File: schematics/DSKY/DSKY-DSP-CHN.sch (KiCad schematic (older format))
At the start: 5 parts, among them U20 74LS273, U21 74LS273, U22 74LS273, U5 74LS04, U7 74LS00

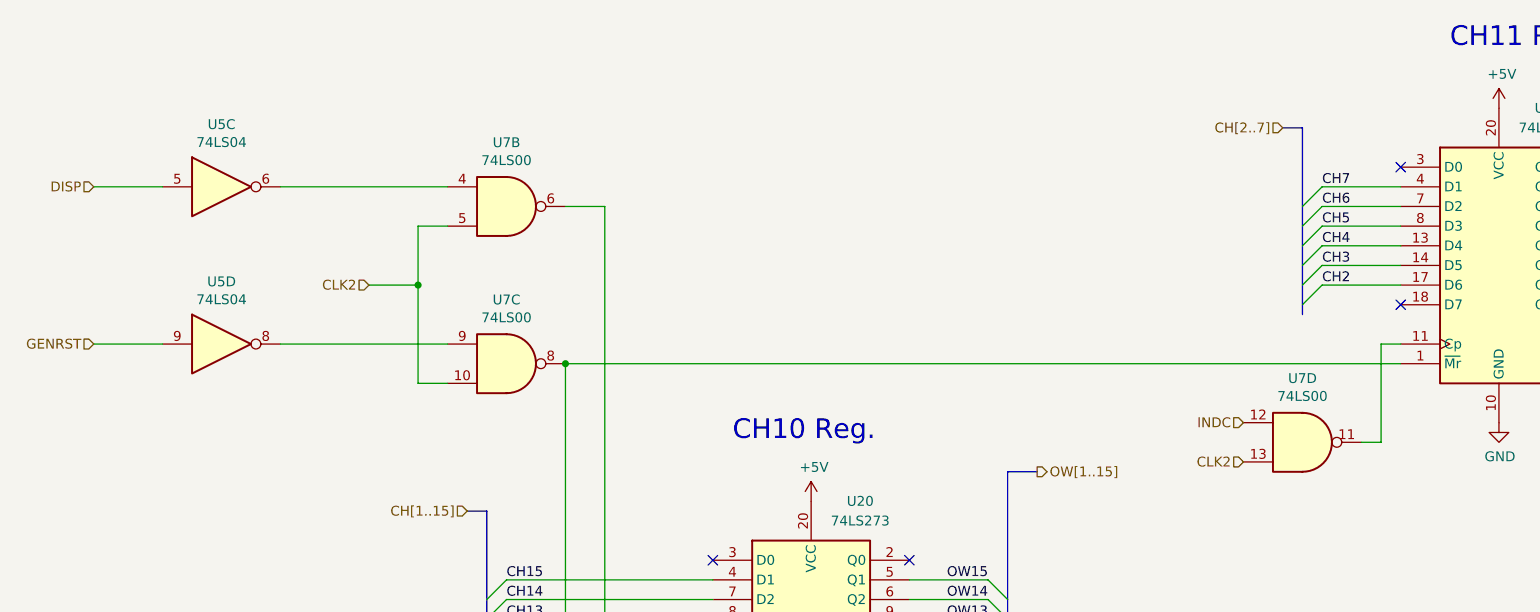
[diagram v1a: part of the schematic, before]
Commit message: Minor tweaks to the display decoding logic.
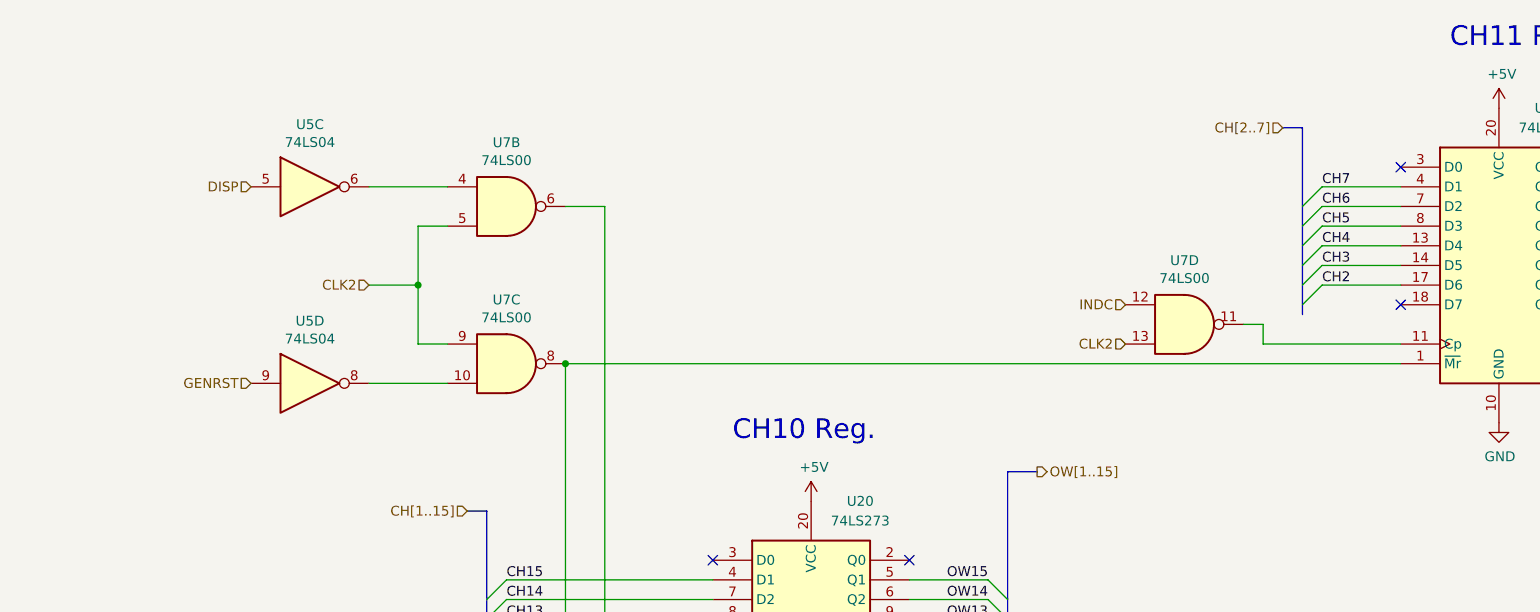
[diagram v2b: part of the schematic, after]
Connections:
- net CLK2: now also U7.9; no longer U7.10
- net at U5.8: now also U7.10; no longer U7.9
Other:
- moved on the sheet: U5C, U5D, U7D
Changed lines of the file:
@@
 	3300 1650 3150 1650
 Wire Wire Line
-	3300 2450 3150 2450
-Wire Wire Line
-	3150 2450 3150 1950
-Wire Wire Line
-	3300 2250 2450 2250
-Wire Wire Line
-	3300 1450 2450 1450
+	3300 2250 3150 2250
+Wire Wire Line
+	3300 2450 2900 2450
+Wire Wire Line
+	3300 1450 2900 1450
 Wire Wire Line
 	3150 1950 2900 1950
@@
 L 74xx:74LS04 U?
 U 3 1 67D9AB30
-P 2150 1450
+P 2600 1450
 AR Path="/60F98A4F/67D9AB30" Ref="U?"  Part="5"
 AR Path="/60F98A64/67D1D986/67D9AB30" Ref="U5"  Part="3"
-F 0 "U5" H 2150 1767 50  0000 C CNN
-F 1 "74LS04" H 2150 1676 50  0000 C CNN
-F 2 "" H 2150 1450 50  0001 C CNN
-F 3 "http://www.ti.com/lit/gpn/sn74ls00" H 2150 1450 50  0001 C CNN
-	3    2150 1450
+F 0 "U5" H 2600 1767 50  0000 C CNN
+F 1 "74LS04" H 2600 1676 50  0000 C CNN
+F 2 "" H 2600 1450 50  0001 C CNN
+F 3 "http://www.ti.com/lit/gpn/sn74ls00" H 2600 1450 50  0001 C CNN
+	3    2600 1450
 	1    0    0    -1
 $EndComp
@@
 L 74xx:74LS04 U?
 U 4 1 67D9AB36
-P 2150 2250
+P 2600 2450
 AR Path="/60F98A4F/67D9AB36" Ref="U?"  Part="6"
 AR Path="/60F98A64/67D1D986/67D9AB36" Ref="U5"  Part="4"
-F 0 "U5" H 2150 2567 50  0000 C CNN
-F 1 "74LS04" H 2150 2476 50  0000 C CNN
-F 2 "" H 2150 2250 50  0001 C CNN
-F 3 "http://www.ti.com/lit/gpn/sn74ls00" H 2150 2250 50  0001 C CNN
-	4    2150 2250
-	1    0    0    -1
-$EndComp
-Wire Wire Line
-	1850 2250 1500 2250
-Wire Wire Line
-	1850 1450 1500 1450
-Text HLabel 1500 1450 0    50   Input ~ 0
+F 0 "U5" H 2600 2767 50  0000 C CNN
+F 1 "74LS04" H 2600 2676 50  0000 C CNN
+F 2 "" H 2600 2450 50  0001 C CNN
+F 3 "http://www.ti.com/lit/gpn/sn74ls00" H 2600 2450 50  0001 C CNN
+	4    2600 2450
+	1    0    0    -1
+$EndComp
+Text HLabel 2300 1450 0    50   Input ~ 0
 DISP
-Text HLabel 1500 2250 0    50   Input ~ 0
+Text HLabel 2300 2450 0    50   Input ~ 0
 GENRST
 Text Notes 4750 2750 0    100  ~ 0
@@
 Connection ~ 3900 2350
 Wire Wire Line
-	8150 2250 8050 2250
-Wire Wire Line
-	8050 2250 8050 2750
-Wire Wire Line
-	8050 2750 7950 2750
+	7450 2150 7350 2150
 $Comp
 L 74xx:74LS00 U?
 U 4 1 78C759B0
-P 7650 2750
+P 7050 2150
 AR Path="/60F98A4F/78C759B0" Ref="U?"  Part="4"
 AR Path="/60F98A64/67D1D986/78C759B0" Ref="U7"  Part="4"
-F 0 "U7" H 7650 3075 50  0000 C CNN
-F 1 "74LS00" H 7650 2984 50  0000 C CNN
-F 2 "" H 7650 2750 50  0001 C CNN
-F 3 "http://www.ti.com/lit/gpn/sn74ls00" H 7650 2750 50  0001 C CNN
-	4    7650 2750
-	1    0    0    -1
-$EndComp
-Text HLabel 7350 2850 0    50   Input ~ 0
+F 0 "U7" H 7050 2475 50  0000 C CNN
+F 1 "74LS00" H 7050 2384 50  0000 C CNN
+F 2 "" H 7050 2150 50  0001 C CNN
+F 3 "http://www.ti.com/lit/gpn/sn74ls00" H 7050 2150 50  0001 C CNN
+	4    7050 2150
+	1    0    0    -1
+$EndComp
+Text HLabel 6750 2250 0    50   Input ~ 0
 CLK2
-Text HLabel 7350 2650 0    50   Input ~ 0
+Text HLabel 6750 2050 0    50   Input ~ 0
 INDC
 NoConn ~ 5650 3350
@@
 Wire Wire Line
 	3900 2350 8150 2350
+Wire Wire Line
+	7450 2250 8150 2250
+Wire Wire Line
+	7450 2150 7450 2250
+Wire Wire Line
+	3150 2250 3150 1950
 Wire Bus Line
 	7650 1150 7650 2100

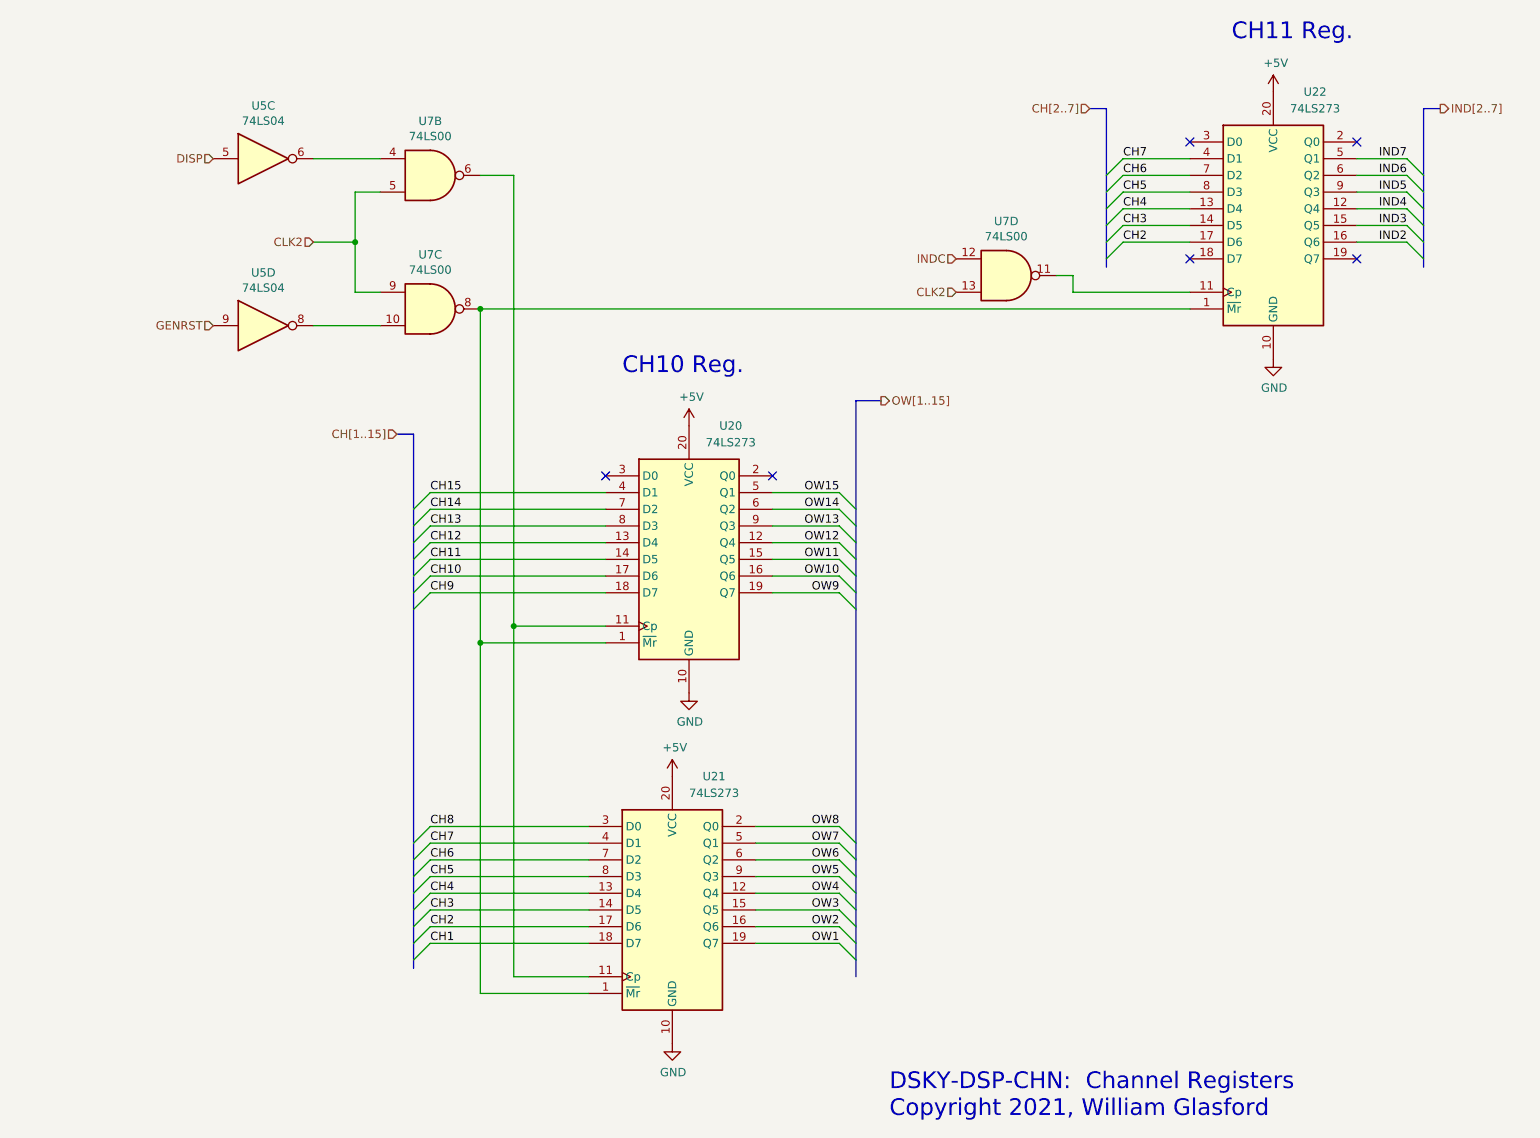
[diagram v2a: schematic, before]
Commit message: Simplified reset lines.
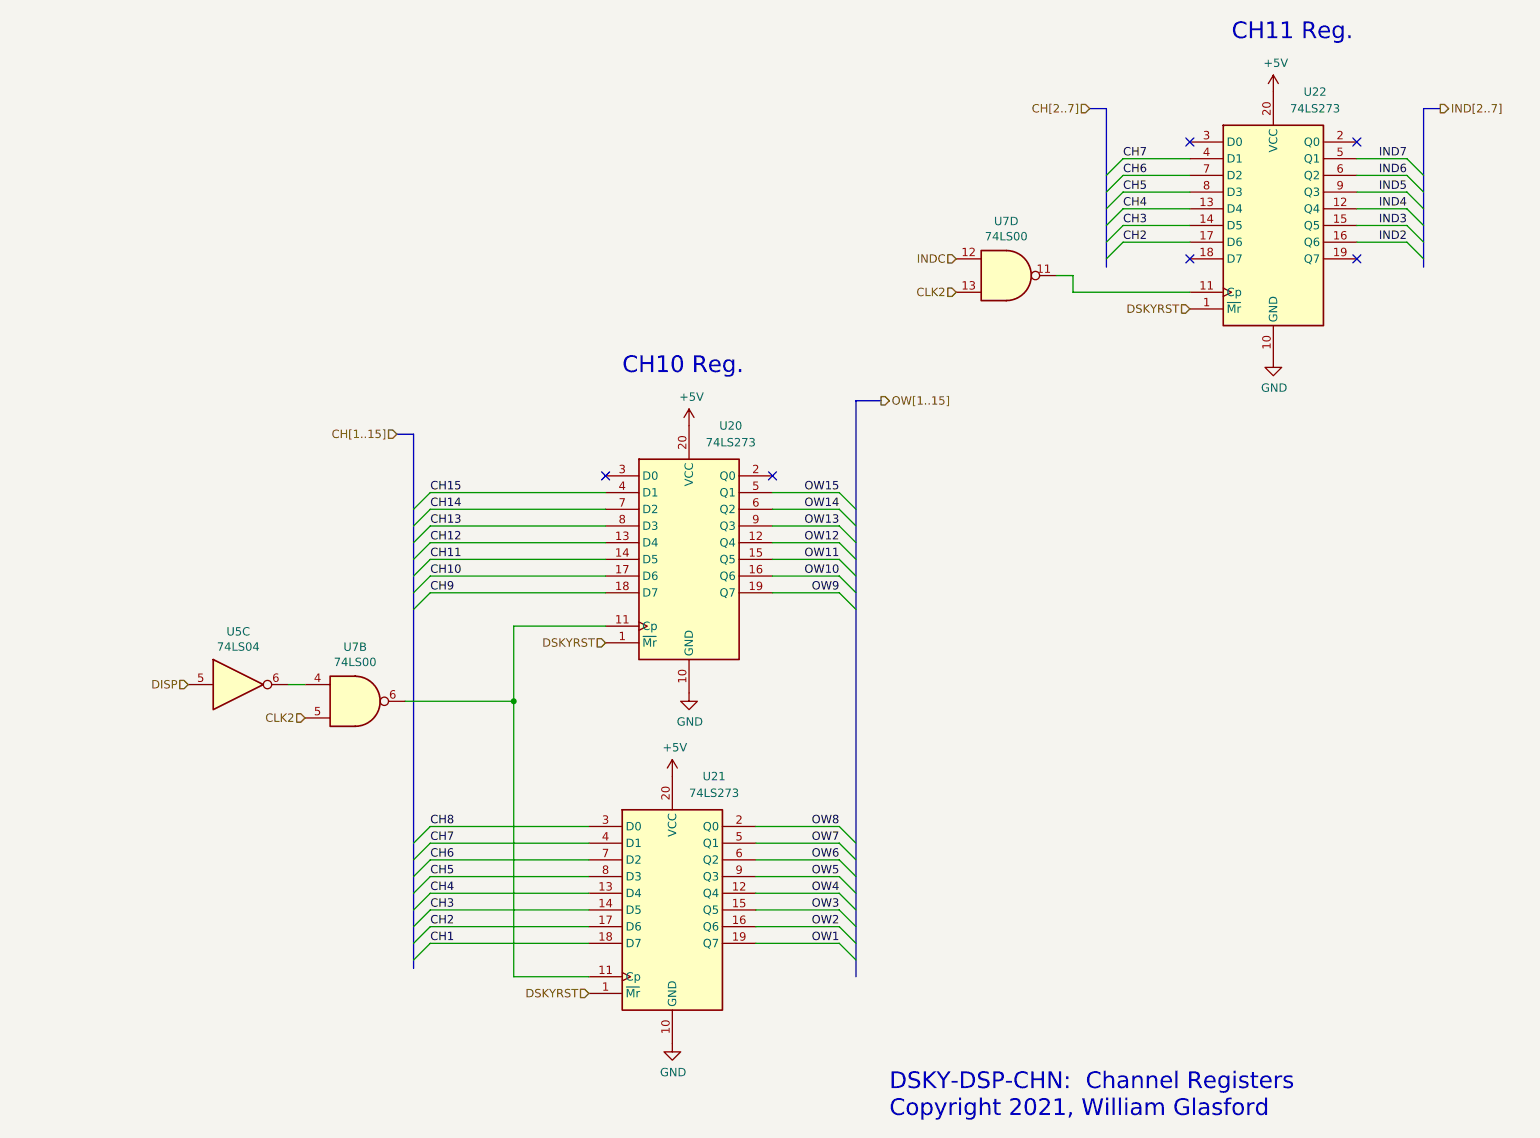
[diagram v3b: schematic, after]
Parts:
- removed unit 4 of U5
- removed unit 3 of U7
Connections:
- net DSKYRST: now reaches U20.1 (~Mr), U21.1 (~Mr), U22.1 (~Mr)
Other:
- moved on the sheet: U5C, U7B
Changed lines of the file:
@@
 L 74xx:74LS00 U?
 U 2 1 67D9AB1B
-P 3600 1550
+P 3150 4700
 AR Path="/60F98A4F/67D9AB1B" Ref="U?"  Part="4"
 AR Path="/60F98A64/67D1D986/67D9AB1B" Ref="U7"  Part="2"
-F 0 "U7" H 3600 1875 50  0000 C CNN
-F 1 "74LS00" H 3600 1784 50  0000 C CNN
-F 2 "" H 3600 1550 50  0001 C CNN
-F 3 "http://www.ti.com/lit/gpn/sn74ls00" H 3600 1550 50  0001 C CNN
-	2    3600 1550
-	1    0    0    -1
-$EndComp
-$Comp
-L 74xx:74LS00 U?
-U 3 1 67D9AB21
-P 3600 2350
-AR Path="/60F98A4F/67D9AB21" Ref="U?"  Part="3"
-AR Path="/60F98A64/67D1D986/67D9AB21" Ref="U7"  Part="3"
-F 0 "U7" H 3600 2675 50  0000 C CNN
-F 1 "74LS00" H 3600 2584 50  0000 C CNN
-F 2 "" H 3600 2350 50  0001 C CNN
-F 3 "http://www.ti.com/lit/gpn/sn74ls00" H 3600 2350 50  0001 C CNN
-	3    3600 2350
-	1    0    0    -1
-$EndComp
-Wire Wire Line
-	3300 1650 3150 1650
-Wire Wire Line
-	3300 2250 3150 2250
-Wire Wire Line
-	3300 2450 2900 2450
-Wire Wire Line
-	3300 1450 2900 1450
-Wire Wire Line
-	3150 1950 2900 1950
-Connection ~ 3150 1950
-Wire Wire Line
-	3150 1950 3150 1650
-Text HLabel 2900 1950 0    50   Input ~ 0
+F 0 "U7" H 3150 5025 50  0000 C CNN
+F 1 "74LS00" H 3150 4934 50  0000 C CNN
+F 2 "" H 3150 4700 50  0001 C CNN
+F 3 "http://www.ti.com/lit/gpn/sn74ls00" H 3150 4700 50  0001 C CNN
+	2    3150 4700
+	1    0    0    -1
+$EndComp
+Wire Wire Line
+	2850 4600 2750 4600
+Text HLabel 2850 4800 0    50   Input ~ 0
 CLK2
 $Comp
 L 74xx:74LS04 U?
 U 3 1 67D9AB30
-P 2600 1450
+P 2450 4600
 AR Path="/60F98A4F/67D9AB30" Ref="U?"  Part="5"
 AR Path="/60F98A64/67D1D986/67D9AB30" Ref="U5"  Part="3"
-F 0 "U5" H 2600 1767 50  0000 C CNN
-F 1 "74LS04" H 2600 1676 50  0000 C CNN
-F 2 "" H 2600 1450 50  0001 C CNN
-F 3 "http://www.ti.com/lit/gpn/sn74ls00" H 2600 1450 50  0001 C CNN
-	3    2600 1450
-	1    0    0    -1
-$EndComp
-$Comp
-L 74xx:74LS04 U?
-U 4 1 67D9AB36
-P 2600 2450
-AR Path="/60F98A4F/67D9AB36" Ref="U?"  Part="6"
-AR Path="/60F98A64/67D1D986/67D9AB36" Ref="U5"  Part="4"
-F 0 "U5" H 2600 2767 50  0000 C CNN
-F 1 "74LS04" H 2600 2676 50  0000 C CNN
-F 2 "" H 2600 2450 50  0001 C CNN
-F 3 "http://www.ti.com/lit/gpn/sn74ls00" H 2600 2450 50  0001 C CNN
-	4    2600 2450
-	1    0    0    -1
-$EndComp
-Text HLabel 2300 1450 0    50   Input ~ 0
+F 0 "U5" H 2450 4917 50  0000 C CNN
+F 1 "74LS04" H 2450 4826 50  0000 C CNN
+F 2 "" H 2450 4600 50  0001 C CNN
+F 3 "http://www.ti.com/lit/gpn/sn74ls00" H 2450 4600 50  0001 C CNN
+	3    2450 4600
+	1    0    0    -1
+$EndComp
+Text HLabel 2150 4600 0    50   Input ~ 0
 DISP
-Text HLabel 2300 2450 0    50   Input ~ 0
-GENRST
+Text HLabel 8150 2350 0    50   Input ~ 0
+DSKYRST
 Text Notes 4750 2750 0    100  ~ 0
 CH10 Reg.
-Connection ~ 3900 4350
-Wire Wire Line
-	3900 4350 3900 6450
-Connection ~ 4100 4250
-Wire Wire Line
-	4100 4250 4100 6350
-Wire Wire Line
-	4650 4350 3900 4350
+Wire Wire Line
+	4100 4250 4100 4700
 Wire Wire Line
 	4650 4250 4100 4250
@@
 $EndComp
 Wire Wire Line
-	4100 1550 4100 4250
-Wire Wire Line
-	3900 2350 3900 4350
-Wire Wire Line
-	4100 1550 3900 1550
+	4100 4700 3450 4700
 Wire Wire Line
 	9450 1450 9150 1450
@@
 	1    0    0    -1
 $EndComp
-Wire Wire Line
-	4550 6450 3900 6450
 $Comp
 L 74xx:74LS273 U?
@@
 Text Label 9450 1450 2    50   ~ 0
 IND7
-Connection ~ 3900 2350
 Wire Wire Line
 	7450 2150 7350 2150
@@
 NoConn ~ 8150 2050
 Wire Wire Line
-	3900 2350 8150 2350
-Wire Wire Line
 	7450 2250 8150 2250
 Wire Wire Line
 	7450 2150 7450 2250
-Wire Wire Line
-	3150 2250 3150 1950
+Text HLabel 4650 4350 0    50   Input ~ 0
+DSKYRST
+Text HLabel 4550 6450 0    50   Input ~ 0
+DSKYRST
+Connection ~ 4100 4700
+Wire Wire Line
+	4100 4700 4100 6350
 Wire Bus Line
 	7650 1150 7650 2100

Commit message: Cleaned up clock logic.
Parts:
- removed U5: 74LS04, symbol 74xx:74LS04
- removed U7: 74LS00, symbol 74xx:74LS00
- renumbered U22 to U20, U20 to U22
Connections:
- net DISP: now also U21.11 (Cp), U22.11 (Cp)
- net INDC: now also U20.11 (Cp)
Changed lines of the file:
@@
 	1    0    0    -1
 $EndComp
-$Comp
-L 74xx:74LS00 U?
-U 2 1 67D9AB1B
-P 3150 4700
-AR Path="/60F98A4F/67D9AB1B" Ref="U?"  Part="4"
-AR Path="/60F98A64/67D1D986/67D9AB1B" Ref="U7"  Part="2"
-F 0 "U7" H 3150 5025 50  0000 C CNN
-F 1 "74LS00" H 3150 4934 50  0000 C CNN
-F 2 "" H 3150 4700 50  0001 C CNN
-F 3 "http://www.ti.com/lit/gpn/sn74ls00" H 3150 4700 50  0001 C CNN
-	2    3150 4700
-	1    0    0    -1
-$EndComp
-Wire Wire Line
-	2850 4600 2750 4600
-Text HLabel 2850 4800 0    50   Input ~ 0
-CLK2
-$Comp
-L 74xx:74LS04 U?
-U 3 1 67D9AB30
-P 2450 4600
-AR Path="/60F98A4F/67D9AB30" Ref="U?"  Part="5"
-AR Path="/60F98A64/67D1D986/67D9AB30" Ref="U5"  Part="3"
-F 0 "U5" H 2450 4917 50  0000 C CNN
-F 1 "74LS04" H 2450 4826 50  0000 C CNN
-F 2 "" H 2450 4600 50  0001 C CNN
-F 3 "http://www.ti.com/lit/gpn/sn74ls00" H 2450 4600 50  0001 C CNN
-	3    2450 4600
-	1    0    0    -1
-$EndComp
-Text HLabel 2150 4600 0    50   Input ~ 0
+Text HLabel 4000 4700 0    50   Input ~ 0
 DISP
 Text HLabel 8150 2350 0    50   Input ~ 0
@@
 P 5150 3850
 AR Path="/60F98A4F/67D9AB75" Ref="U?"  Part="1"
-AR Path="/60F98A64/67D1D986/67D9AB75" Ref="U20"  Part="1"
-F 0 "U20" H 5400 4650 50  0000 C CNN
+AR Path="/60F98A64/67D1D986/67D9AB75" Ref="U22"  Part="1"
+F 0 "U22" H 5400 4650 50  0000 C CNN
 F 1 "74LS273" H 5400 4550 50  0000 C CNN
 F 2 "" H 5150 3850 50  0001 C CNN
@@
 $EndComp
 Wire Wire Line
-	4100 4700 3450 4700
+	4100 4700 4000 4700
 Wire Wire Line
 	9450 1450 9150 1450
@@
 P 8650 1850
 AR Path="/60F98A4F/67EF035A" Ref="U?"  Part="1"
-AR Path="/60F98A64/67D1D986/67EF035A" Ref="U22"  Part="1"
-F 0 "U22" H 8900 2650 50  0000 C CNN
+AR Path="/60F98A64/67D1D986/67EF035A" Ref="U20"  Part="1"
+F 0 "U20" H 8900 2650 50  0000 C CNN
 F 1 "74LS273" H 8900 2550 50  0000 C CNN
 F 2 "" H 8650 1850 50  0001 C CNN
@@
 Text Label 9450 1450 2    50   ~ 0
 IND7
-Wire Wire Line
-	7450 2150 7350 2150
-$Comp
-L 74xx:74LS00 U?
-U 4 1 78C759B0
-P 7050 2150
-AR Path="/60F98A4F/78C759B0" Ref="U?"  Part="4"
-AR Path="/60F98A64/67D1D986/78C759B0" Ref="U7"  Part="4"
-F 0 "U7" H 7050 2475 50  0000 C CNN
-F 1 "74LS00" H 7050 2384 50  0000 C CNN
-F 2 "" H 7050 2150 50  0001 C CNN
-F 3 "http://www.ti.com/lit/gpn/sn74ls00" H 7050 2150 50  0001 C CNN
-	4    7050 2150
-	1    0    0    -1
-$EndComp
-Text HLabel 6750 2250 0    50   Input ~ 0
-CLK2
-Text HLabel 6750 2050 0    50   Input ~ 0
+Text HLabel 8150 2250 0    50   Input ~ 0
 INDC
 NoConn ~ 5650 3350
@@
 NoConn ~ 9150 2050
 NoConn ~ 8150 2050
-Wire Wire Line
-	7450 2250 8150 2250
-Wire Wire Line
-	7450 2150 7450 2250
 Text HLabel 4650 4350 0    50   Input ~ 0
 DSKYRST

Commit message: Sign processing overhauled.
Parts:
- added U5: 74LS04, symbol 74xx:74LS04
- added U7: 74LS08, symbol 74xx:74LS08
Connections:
- net DISP: now also U7.4; no longer U21.11 (Cp), U22.11 (Cp)
- net INDC: now also U5.9; no longer U20.11 (Cp)
- new net: U20.11 (Cp), U7.11
- new net: U5.8, U7.12
- new net: U21.11 (Cp), U22.11 (Cp), U7.6
- new net CLK2: U7.13, U7.5
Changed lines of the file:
@@
 $Descr A 11000 8500
 encoding utf-8
-Sheet 4 10
+Sheet 4 11
 Title ""
 Date ""
@@
 	1    0    0    -1
 $EndComp
-Text HLabel 4000 4700 0    50   Input ~ 0
+Text HLabel 2800 4600 0    50   Input ~ 0
 DISP
 Text HLabel 8150 2350 0    50   Input ~ 0
@@
 $EndComp
 Wire Wire Line
-	4100 4700 4000 4700
+	4100 4700 3400 4700
 Wire Wire Line
 	9450 1450 9150 1450
@@
 Text Label 9450 1450 2    50   ~ 0
 IND7
-Text HLabel 8150 2250 0    50   Input ~ 0
+Text HLabel 6400 2150 0    50   Input ~ 0
 INDC
 NoConn ~ 5650 3350
@@
 Wire Wire Line
 	4100 4700 4100 6350
+$Comp
+L 74xx:74LS08 U7
+U 4 1 61B5C630
+P 7300 2250
+F 0 "U7" H 7300 2575 50  0000 C CNN
+F 1 "74LS08" H 7300 2484 50  0000 C CNN
+F 2 "" H 7300 2250 50  0001 C CNN
+F 3 "http://www.ti.com/lit/gpn/sn74LS08" H 7300 2250 50  0001 C CNN
+	4    7300 2250
+	1    0    0    -1
+$EndComp
+$Comp
+L 74xx:74LS08 U7
+U 2 1 61B5DD51
+P 3100 4700
+F 0 "U7" H 3100 5025 50  0000 C CNN
+F 1 "74LS08" H 3100 4934 50  0000 C CNN
+F 2 "" H 3100 4700 50  0001 C CNN
+F 3 "http://www.ti.com/lit/gpn/sn74LS08" H 3100 4700 50  0001 C CNN
+	2    3100 4700
+	1    0    0    -1
+$EndComp
+Wire Wire Line
+	7600 2250 8150 2250
+Text HLabel 2800 4800 0    50   Input ~ 0
+CLK2
+Text HLabel 7000 2350 0    50   Input ~ 0
+CLK2
+$Comp
+L 74xx:74LS04 U5
+U 4 1 61B646F9
+P 6700 2150
+F 0 "U5" H 6700 2467 50  0000 C CNN
+F 1 "74LS04" H 6700 2376 50  0000 C CNN
+F 2 "" H 6700 2150 50  0001 C CNN
+F 3 "http://www.ti.com/lit/gpn/sn74LS04" H 6700 2150 50  0001 C CNN
+	4    6700 2150
+	1    0    0    -1
+$EndComp
 Wire Bus Line
 	7650 1150 7650 2100
